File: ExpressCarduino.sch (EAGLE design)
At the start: 15 parts, among them IC2 MCP23008, U1 AP3012

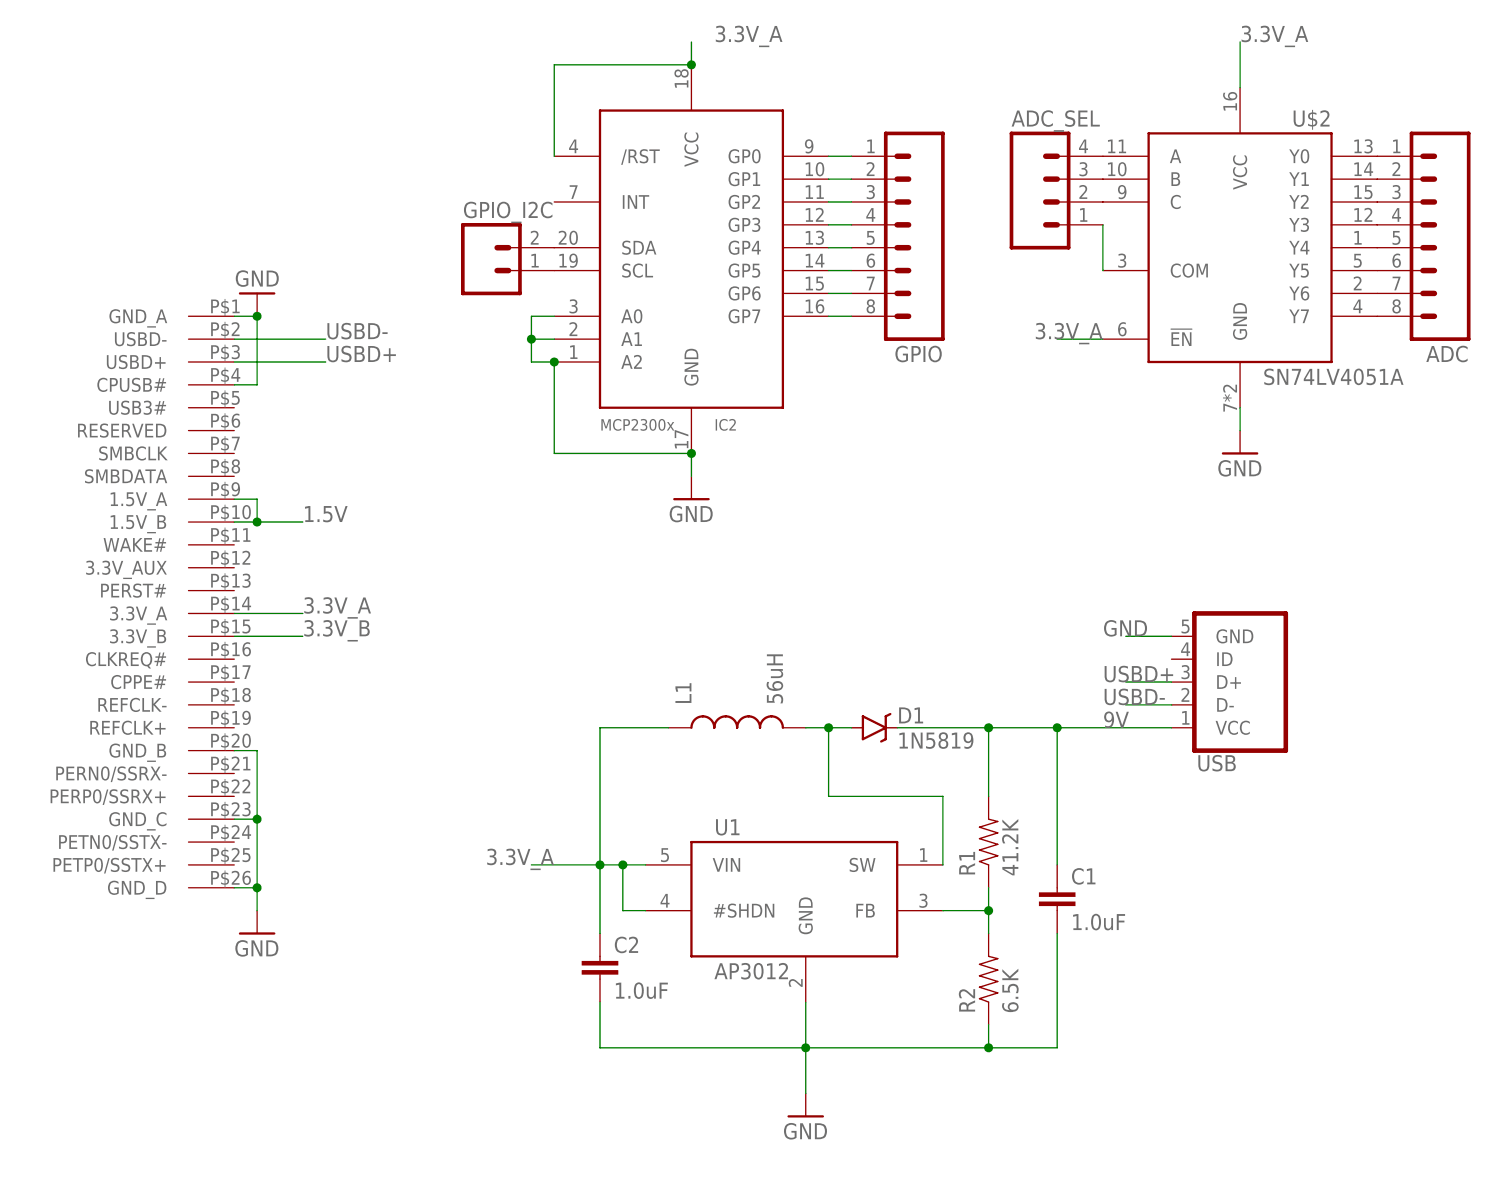
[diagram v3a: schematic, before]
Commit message: Isolated the USB circuit from the other ICs
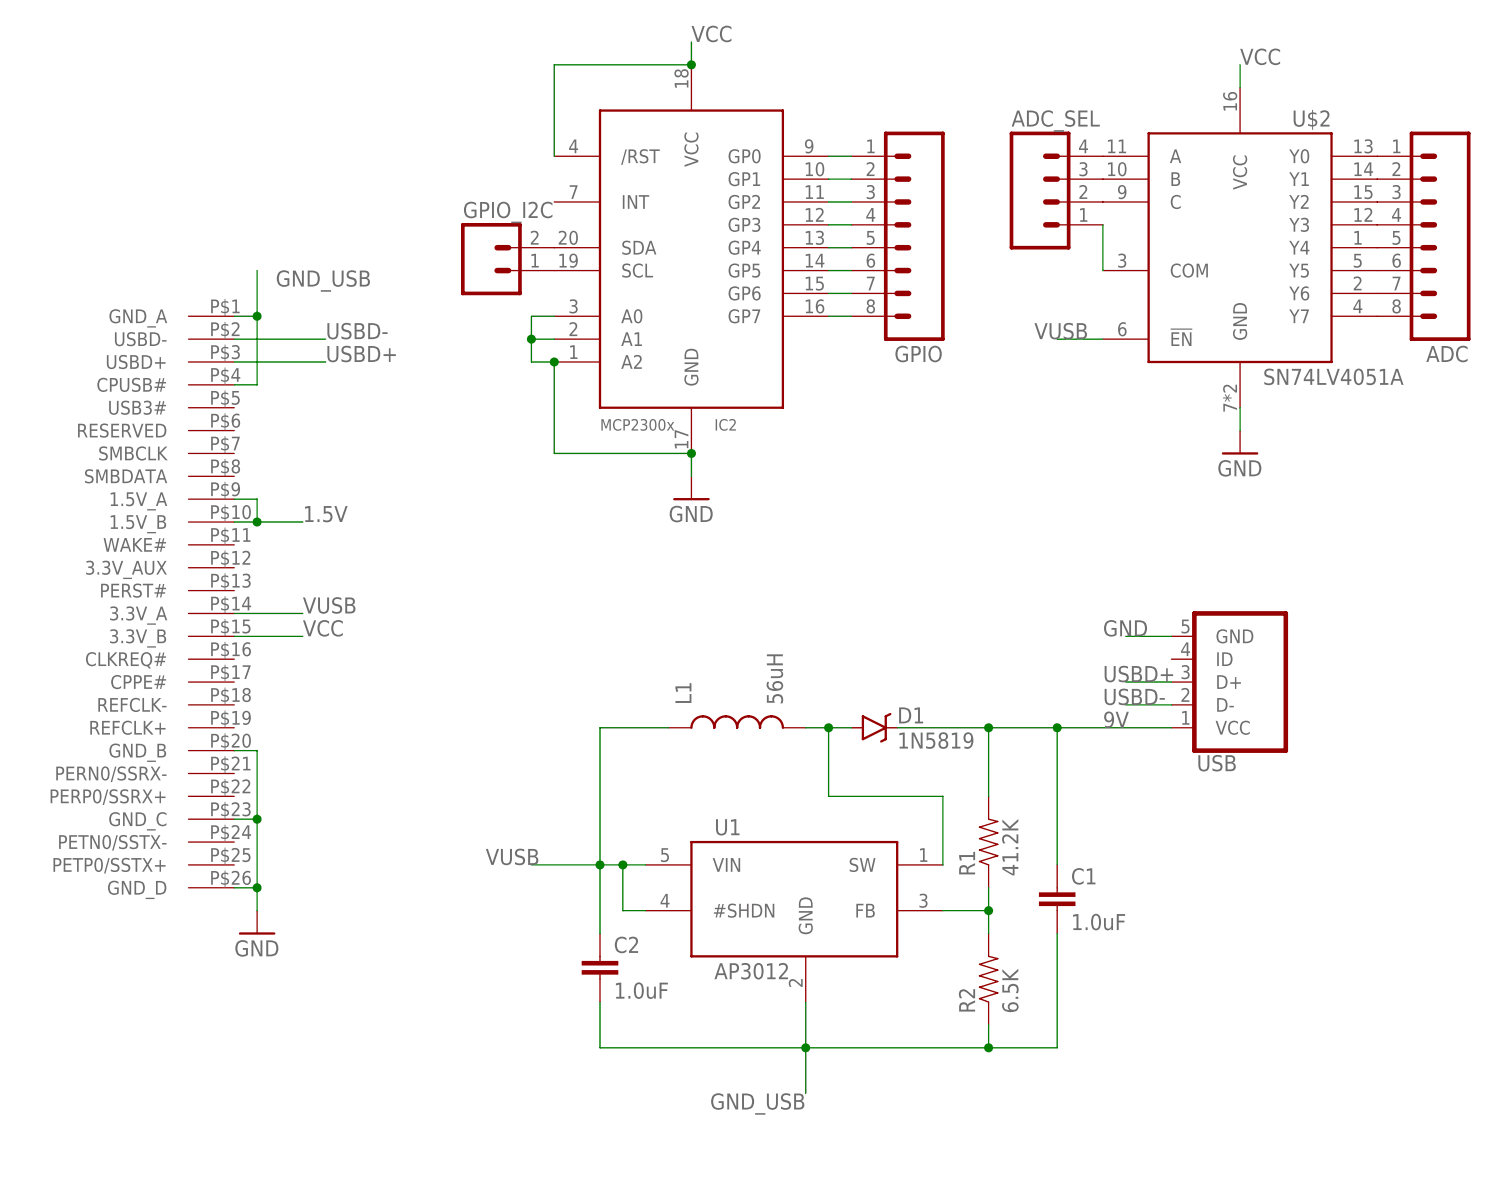
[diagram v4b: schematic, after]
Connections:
- removed net 3.3V_A: C2.1, IC2./RST, IC2.VCC, L1.1, U$1.3.3V_A, U$2.!EN, U$2.VCC, U1.#SHDN, U1.VIN
- removed net 3.3V_B: U$1.3.3V_B
- new net GND_USB: C1.2, C2.2, R2.1, U$1.CPUSB#, U$1.GND_A, U1.GND
- new net VCC: IC2./RST, IC2.VCC, U$1.3.3V_B, U$2.VCC
- new net VUSB: C2.1, L1.1, U$1.3.3V_A, U$2.!EN, U1.#SHDN, U1.VIN
- net GND: no longer C1.2, C2.2, R2.1, U$1.CPUSB#, U$1.GND_A, U1.GND
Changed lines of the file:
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@@
 <part name="GND1" library="supply1" deviceset="GND" device=""/>
 <part name="U1" library="HokieGeek" deviceset="AP3012" device="" value="AP3012"/>
-<part name="GND2" library="supply1" deviceset="GND" device=""/>
 <part name="C1" library="SparkFun-Capacitors" deviceset="1.0UF-16V-10%(0603)" device="" value="1.0uF"/>
 <part name="C2" library="SparkFun-Capacitors" deviceset="1.0UF-16V-10%(0603)" device="" value="1.0uF"/>
@@
 <part name="D1" library="HokieGeek" deviceset="DIODE-SCHOTTKY" device="" value="1N5819"/>
 <part name="USB" library="HokieGeek" deviceset="USB_MICROB_PLUG" device="&quot;"/>
-<part name="GND3" library="supply1" deviceset="GND" device=""/>
 <part name="GND4" library="supply1" deviceset="GND" device=""/>
 <part name="GND5" library="supply1" deviceset="GND" device=""/>
@@
 <instance part="GND1" gate="1" x="17.78" y="22.86"/>
 <instance part="U1" gate="G$1" x="73.66" y="25.4"/>
-<instance part="GND2" gate="1" x="78.74" y="2.54"/>
 <instance part="C1" gate="G$1" x="106.68" y="25.4"/>
 <instance part="C2" gate="G$1" x="55.88" y="17.78"/>
@@
 <instance part="D1" gate="G$1" x="86.36" y="45.72"/>
 <instance part="USB" gate="G$1" x="127" y="50.8" rot="MR180"/>
-<instance part="GND3" gate="1" x="17.78" y="93.98" rot="R180"/>
 <instance part="GND4" gate="1" x="66.04" y="71.12"/>
 <instance part="GND5" gate="1" x="127" y="76.2"/>
@@
 </busses>
 <nets>
-<net name="3.3V_B" class="0">
+<net name="VCC" class="0">
 <segment>
 <pinref part="U$1" gate="G$1" pin="3.3V_B"/>
@@
 <label x="22.86" y="55.88" size="1.778" layer="95"/>
 </segment>
+<segment>
+<pinref part="U$2" gate="G$1" pin="VCC"/>
+<wire x1="127" y1="116.84" x2="127" y2="119.38" width="0.1524" layer="91"/>
+<label x="127" y="119.38" size="1.778" layer="95"/>
+</segment>
+<segment>
+<pinref part="IC2" gate="G$1" pin="VCC"/>
+<wire x1="66.04" y1="119.38" x2="66.04" y2="121.92" width="0.1524" layer="91"/>
+<label x="66.04" y="121.92" size="1.778" layer="95"/>
+<junction x="66.04" y="119.38"/>
+<pinref part="IC2" gate="G$1" pin="/RST"/>
+<wire x1="66.04" y1="119.38" x2="50.8" y2="119.38" width="0.1524" layer="91"/>
+<wire x1="50.8" y1="119.38" x2="50.8" y2="109.22" width="0.1524" layer="91"/>
+</segment>
 </net>
 <net name="USBD-" class="0">
@@
 </net>
 <net name="GND" class="0">
-<segment>
-<pinref part="U$1" gate="G$1" pin="CPUSB#"/>
-<wire x1="15.24" y1="83.82" x2="17.78" y2="83.82" width="0.1524" layer="91"/>
-<pinref part="U$1" gate="G$1" pin="GND_A"/>
-<wire x1="15.24" y1="91.44" x2="17.78" y2="91.44" width="0.1524" layer="91"/>
-<wire x1="17.78" y1="83.82" x2="17.78" y2="91.44" width="0.1524" layer="91"/>
-<pinref part="GND3" gate="1" pin="GND"/>
-<junction x="17.78" y="91.44"/>
-</segment>
 <segment>
 <pinref part="U$1" gate="G$1" pin="GND_D"/>
@@
 <junction x="17.78" y="27.94"/>
 <pinref part="GND1" gate="1" pin="GND"/>
-</segment>
-<segment>
-<pinref part="U1" gate="G$1" pin="GND"/>
-<pinref part="GND2" gate="1" pin="GND"/>
-<wire x1="78.74" y1="5.08" x2="78.74" y2="10.16" width="0.1524" layer="91"/>
-<pinref part="C1" gate="G$1" pin="2"/>
-<wire x1="78.74" y1="10.16" x2="78.74" y2="15.24" width="0.1524" layer="91"/>
-<wire x1="106.68" y1="10.16" x2="106.68" y2="22.86" width="0.1524" layer="91"/>
-<pinref part="R2" gate="G$1" pin="1"/>
-<wire x1="99.06" y1="12.7" x2="99.06" y2="10.16" width="0.1524" layer="91"/>
-<wire x1="99.06" y1="10.16" x2="106.68" y2="10.16" width="0.1524" layer="91"/>
-<wire x1="99.06" y1="10.16" x2="78.74" y2="10.16" width="0.1524" layer="91"/>
-<junction x="78.74" y="10.16"/>
-<junction x="99.06" y="10.16"/>
-<pinref part="C2" gate="G$1" pin="2"/>
-<wire x1="78.74" y1="10.16" x2="55.88" y2="10.16" width="0.1524" layer="91"/>
-<wire x1="55.88" y1="10.16" x2="55.88" y2="15.24" width="0.1524" layer="91"/>
 </segment>
 <segment>
@@
 </segment>
 </net>
-<net name="3.3V_A" class="0">
+<net name="VUSB" class="0">
 <segment>
 <pinref part="U$1" gate="G$1" pin="3.3V_A"/>
@@
 </segment>
 <segment>
-<wire x1="66.04" y1="119.38" x2="66.04" y2="121.92" width="0.1524" layer="91"/>
-<label x="68.58" y="121.92" size="1.778" layer="95"/>
-<pinref part="IC2" gate="G$1" pin="VCC"/>
-<pinref part="IC2" gate="G$1" pin="/RST"/>
-<wire x1="66.04" y1="119.38" x2="50.8" y2="119.38" width="0.1524" layer="91"/>
-<wire x1="50.8" y1="119.38" x2="50.8" y2="109.22" width="0.1524" layer="91"/>
-<junction x="66.04" y="119.38"/>
-</segment>
-<segment>
-<wire x1="127" y1="116.84" x2="127" y2="121.92" width="0.1524" layer="91"/>
-<label x="127" y="121.92" size="1.778" layer="95"/>
-<pinref part="U$2" gate="G$1" pin="VCC"/>
-</segment>
-<segment>
 <pinref part="U$2" gate="G$1" pin="!EN"/>
 <wire x1="111.76" y1="88.9" x2="106.68" y2="88.9" width="0.1524" layer="91"/>
@@
 </segment>
 </net>
+<net name="GND_USB" class="0">
+<segment>
+<pinref part="U1" gate="G$1" pin="GND"/>
+<wire x1="78.74" y1="5.08" x2="78.74" y2="10.16" width="0.1524" layer="91"/>
+<pinref part="C1" gate="G$1" pin="2"/>
+<wire x1="78.74" y1="10.16" x2="78.74" y2="15.24" width="0.1524" layer="91"/>
+<wire x1="106.68" y1="10.16" x2="106.68" y2="22.86" width="0.1524" layer="91"/>
+<pinref part="R2" gate="G$1" pin="1"/>
+<wire x1="99.06" y1="12.7" x2="99.06" y2="10.16" width="0.1524" layer="91"/>
+<wire x1="99.06" y1="10.16" x2="106.68" y2="10.16" width="0.1524" layer="91"/>
+<wire x1="99.06" y1="10.16" x2="78.74" y2="10.16" width="0.1524" layer="91"/>
+<junction x="78.74" y="10.16"/>
+<junction x="99.06" y="10.16"/>
+<pinref part="C2" gate="G$1" pin="2"/>
+<wire x1="78.74" y1="10.16" x2="55.88" y2="10.16" width="0.1524" layer="91"/>
+<wire x1="55.88" y1="10.16" x2="55.88" y2="15.24" width="0.1524" layer="91"/>
+<label x="78.74" y="5.08" size="1.778" layer="95" rot="R180"/>
+</segment>
+<segment>
+<pinref part="U$1" gate="G$1" pin="GND_A"/>
+<wire x1="15.24" y1="91.44" x2="17.78" y2="91.44" width="0.1524" layer="91"/>
+<wire x1="17.78" y1="91.44" x2="17.78" y2="96.52" width="0.1524" layer="91"/>
+<junction x="17.78" y="91.44"/>
+<pinref part="U$1" gate="G$1" pin="CPUSB#"/>
+<wire x1="15.24" y1="83.82" x2="17.78" y2="83.82" width="0.1524" layer="91"/>
+<wire x1="17.78" y1="91.44" x2="17.78" y2="83.82" width="0.1524" layer="91"/>
+<label x="30.48" y="96.52" size="1.778" layer="95" rot="R180"/>
+</segment>
+</net>
 </nets>
 </sheet>
 </sheets>
+<errors>
+</errors>
 </schematic>
 </drawing>

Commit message: Updated with correct measurements for the USB plug and swaped out the 8bit expander for the 16
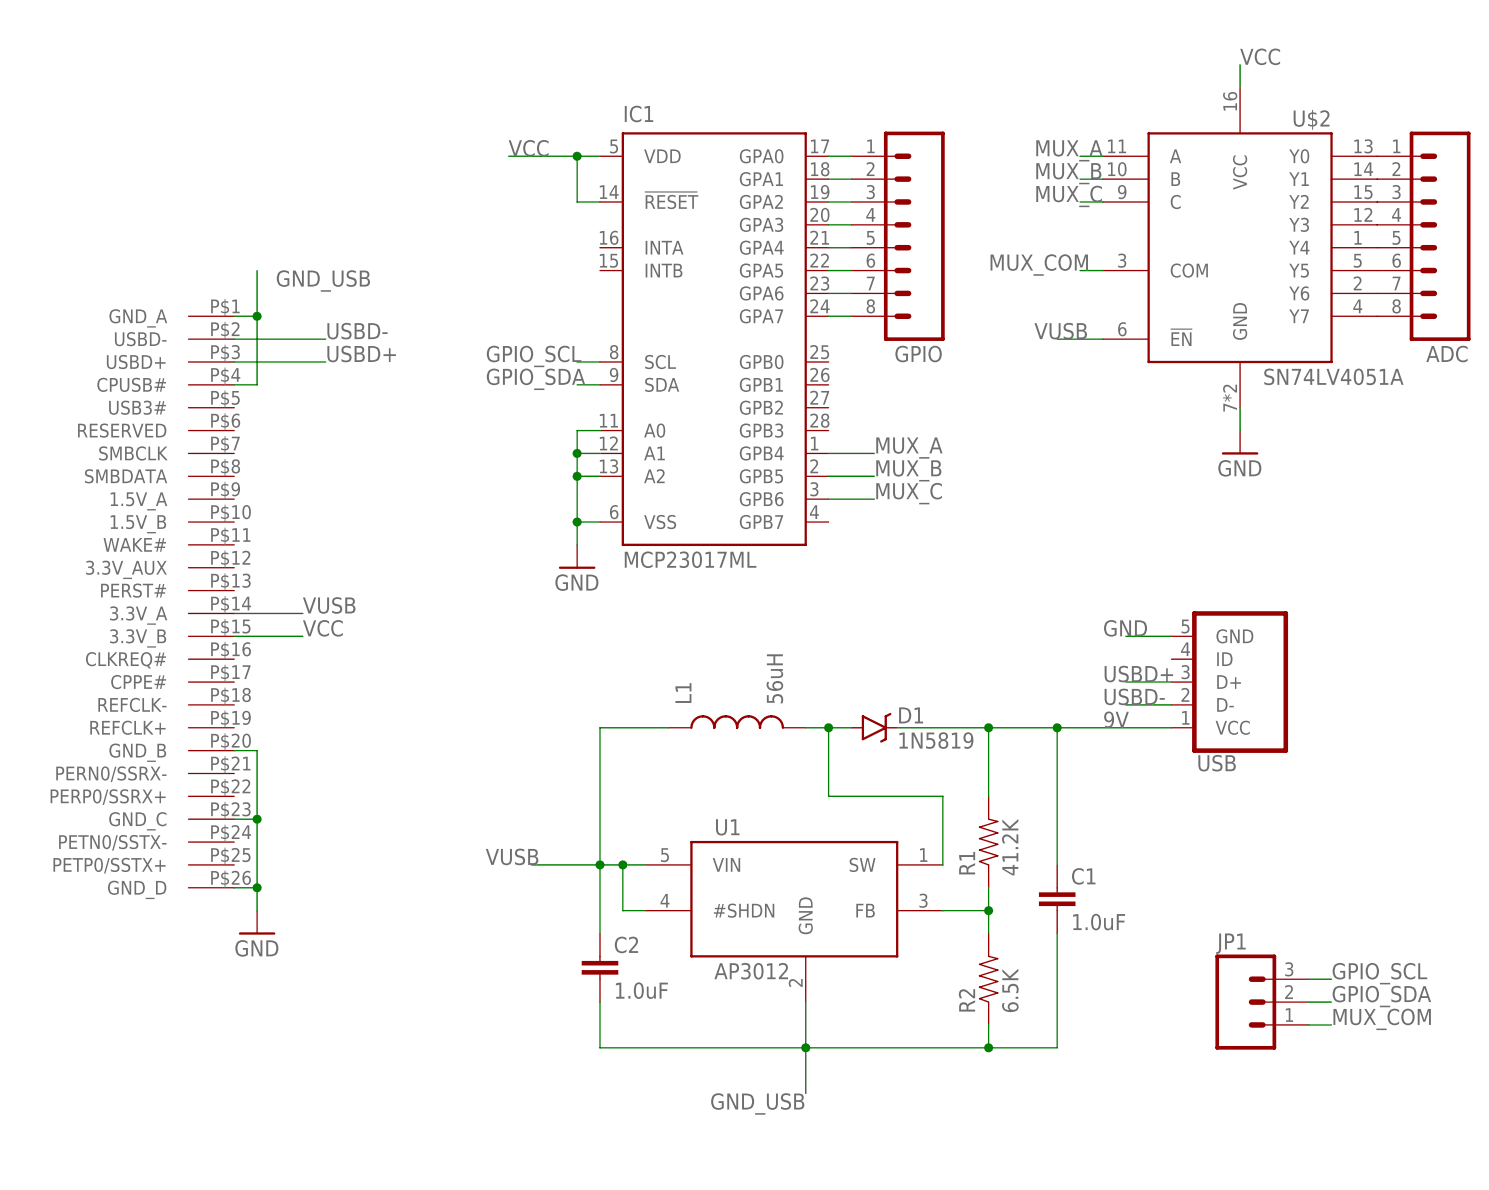
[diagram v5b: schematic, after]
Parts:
- removed ADC_SEL: (no value), SparkFun-Connectors:M04PTH
- removed GPIO_I2C: (no value), SparkFun-Connectors:M02PTH
- removed IC2: MCP23008, HokieGeek:MCP23008
- added IC1: MCP23017ML, adafruit:MCP23017ML
- added JP1: (no value), SparkFun-Connectors:M03PTH
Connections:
- removed net 1.5V: U$1.1.5V_A, U$1.1.5V_B
- removed net N$11: GPIO_I2C.1, IC2.SCL
- removed net N$12: GPIO_I2C.2, IC2.SDA
- removed net N$13: ADC_SEL.1, U$2.COM
- removed net N$29: ADC_SEL.2, U$2.C
- removed net N$30: ADC_SEL.3, U$2.B
- removed net N$31: ADC_SEL.4, U$2.A
- new net GPIO_SCL: IC1.SCL, JP1.3
- new net GPIO_SDA: IC1.SDA, JP1.2
- new net MUX_A: IC1.GPB4, U$2.A
- new net MUX_B: IC1.GPB5, U$2.B
- new net MUX_C: IC1.GPB6, U$2.C
- new net MUX_COM: JP1.1, U$2.COM
- net GND: now also IC1.A0, IC1.A1, IC1.A2, IC1.VSS; no longer IC2.A0, IC2.A1, IC2.A2, IC2.GND
- net N$10: now also IC1.GPA7; no longer IC2.GP7
- net N$2: now also IC1.GPA0; no longer IC2.GP0
- net N$4: now also IC1.GPA1; no longer IC2.GP1
- net N$5: now also IC1.GPA2; no longer IC2.GP2
- net N$6: now also IC1.GPA3; no longer IC2.GP3
- net N$7: now also IC1.GPA4; no longer IC2.GP4
- net N$8: now also IC1.GPA5; no longer IC2.GP5
- net N$9: now also IC1.GPA6; no longer IC2.GP6
- net VCC: now also IC1.!RESET, IC1.VDD; no longer IC2./RST, IC2.VCC
